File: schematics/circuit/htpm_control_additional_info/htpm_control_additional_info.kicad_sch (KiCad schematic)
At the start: 63 parts, among them J1 Conn_01x10_Socket, J2 Conn_01x04_Socket, J3 Conn_01x04_Socket, J4 Conn_01x08_Socket, J5 Conn_01x08_Socket, J6 Conn_01x04_Socket, J7 Conn_01x04_Socket, J8 Conn_01x08_Socket, U1 L7805, U2 74HC595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

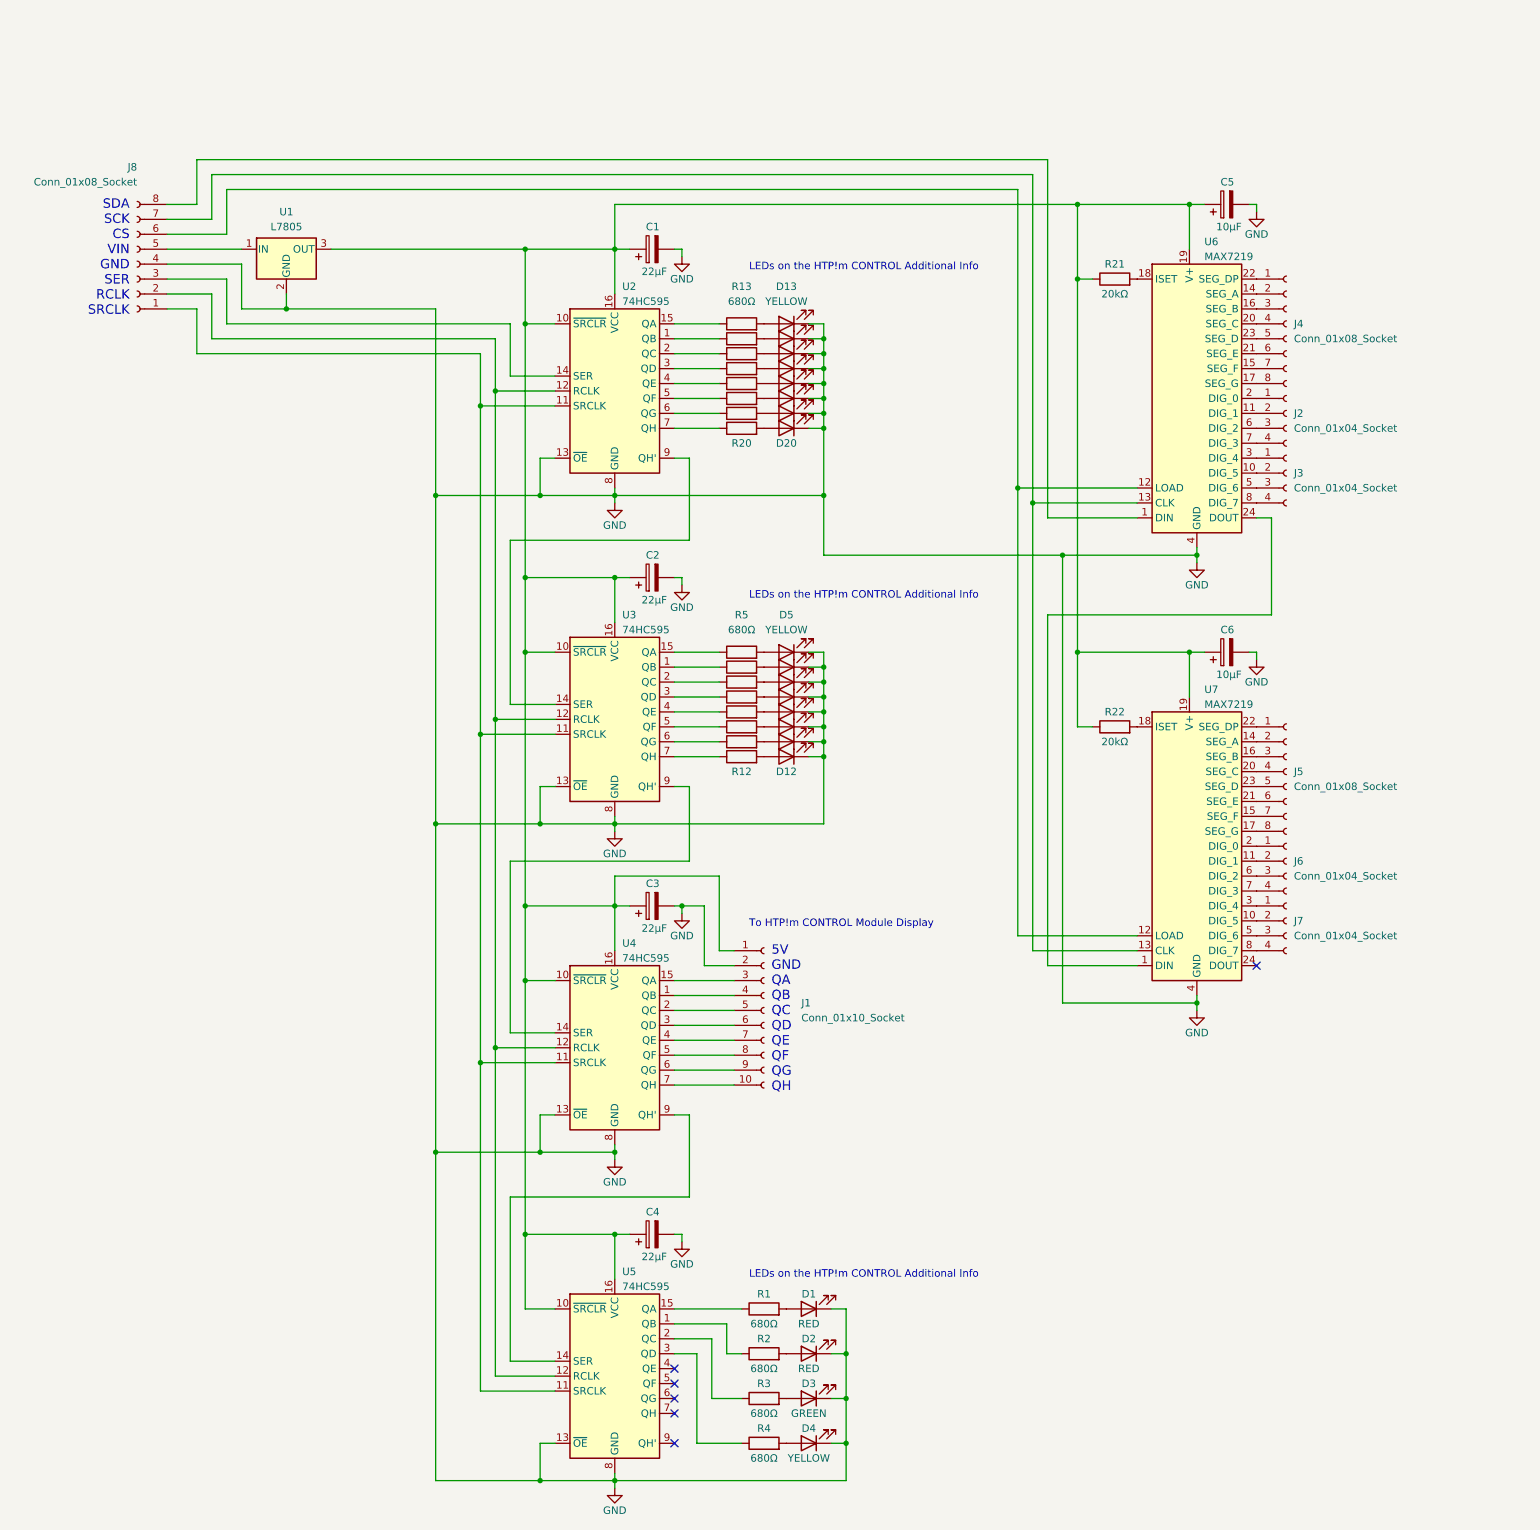
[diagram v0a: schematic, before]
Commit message: Created HTPm CONTROL Additional Info PCB.
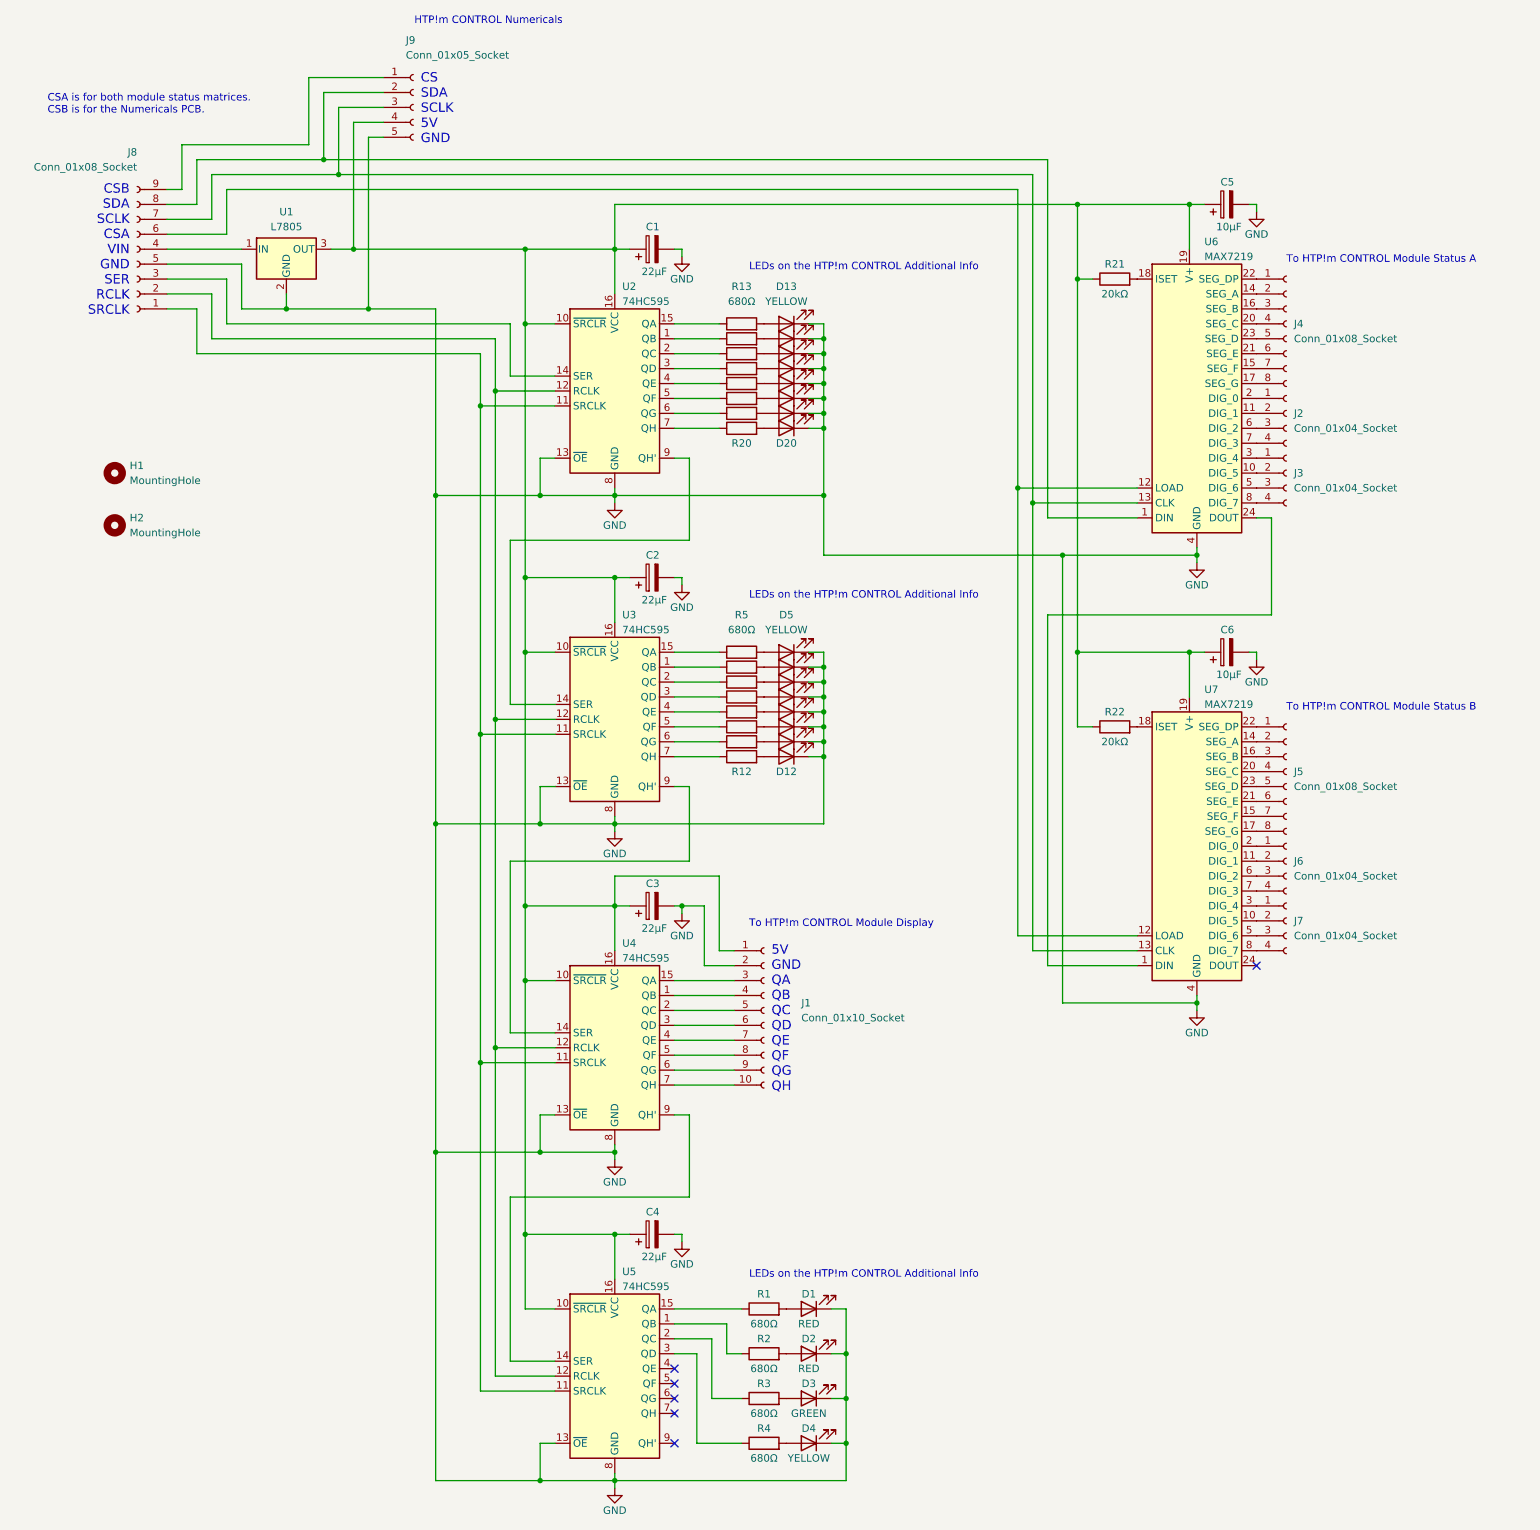
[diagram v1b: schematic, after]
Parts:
- added H1, H2: MountingHole, MountingHole:MountingHole_2.5mm, symbol Mechanical:MountingHole
- added J9: Conn_01x05_Socket, Connector_PinHeader_2.00mm:PinHeader_1x05_P2.00mm_Vertical, symbol Connector:Conn_01x05_Socket
- J8: footprint Connector_PinHeader_2.00mm:PinHeader_1x08_P2.00mm_Vertical -> Connector_PinHeader_2.00mm:PinHeader_1x09_P2.00mm_Vertical; symbol Connector:Conn_01x08_Socket -> Connector:Conn_01x09_Socket
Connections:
- net GND: now also J8.5 (Pin_5), J9.5 (Pin_5); no longer J8.4 (Pin_4)
- net at C1.1, C2.1, C3.1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: now also J9.4 (Pin_4)
- net at J8.7 (Pin_7), U6.13 (CLK), U7.13 (CLK): now also J9.3 (Pin_3)
- net at J8.8 (Pin_8), U6.1 (DIN): now also J9.2 (Pin_2)
- net at U1.1 (IN): now also J8.4 (Pin_4); no longer J8.5 (Pin_5)
- new net: J8.9 (Pin_9), J9.1 (Pin_1)
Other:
- note added: "CS SDA SCLK 5V GND"
- note added: "CSA is for both module status matrices. CSB is for the Numericals PCB."
- note added: "CSB SDA SCLK CSA VIN GND SER RCLK SRCLK"
- note added: "HTP!m CONTROL Numericals"
- note added: "To HTP!m CONTROL Module Status A"
- note added: "To HTP!m CONTROL Module Status B"
- note removed: "SDA SCK CS VIN GND SER RCLK SRCLK"
